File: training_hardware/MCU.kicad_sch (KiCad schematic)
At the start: 2 parts, among them J1 RJ45_LED_Shielded, U1 Teensy4.1_DEV-16771

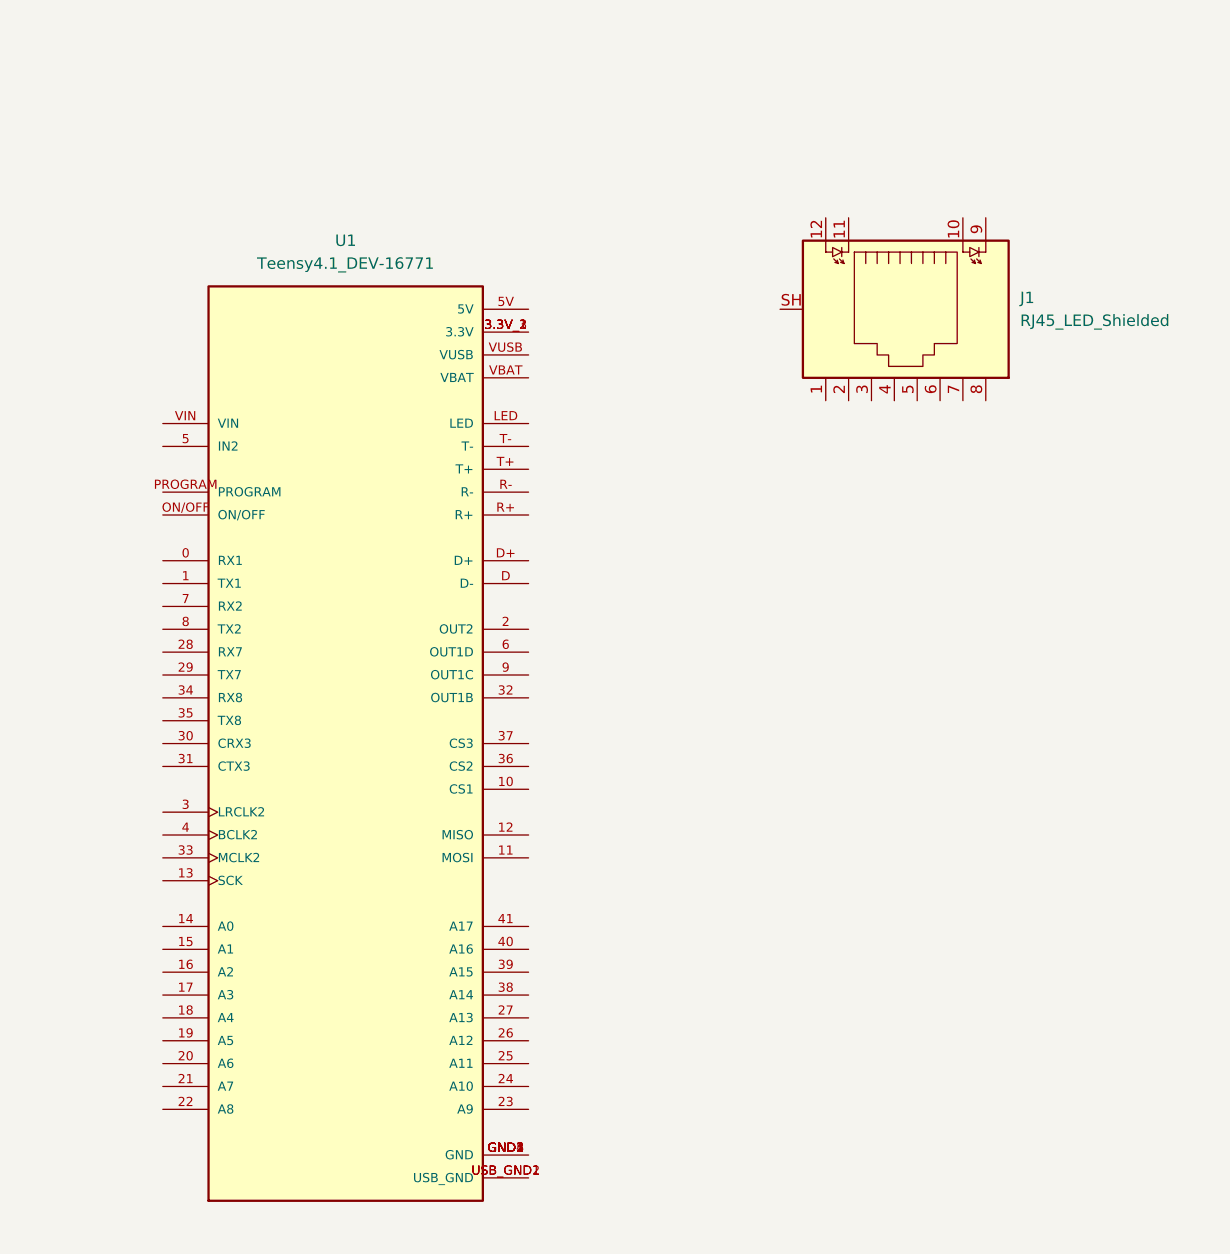
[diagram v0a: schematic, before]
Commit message: Add Ethernet
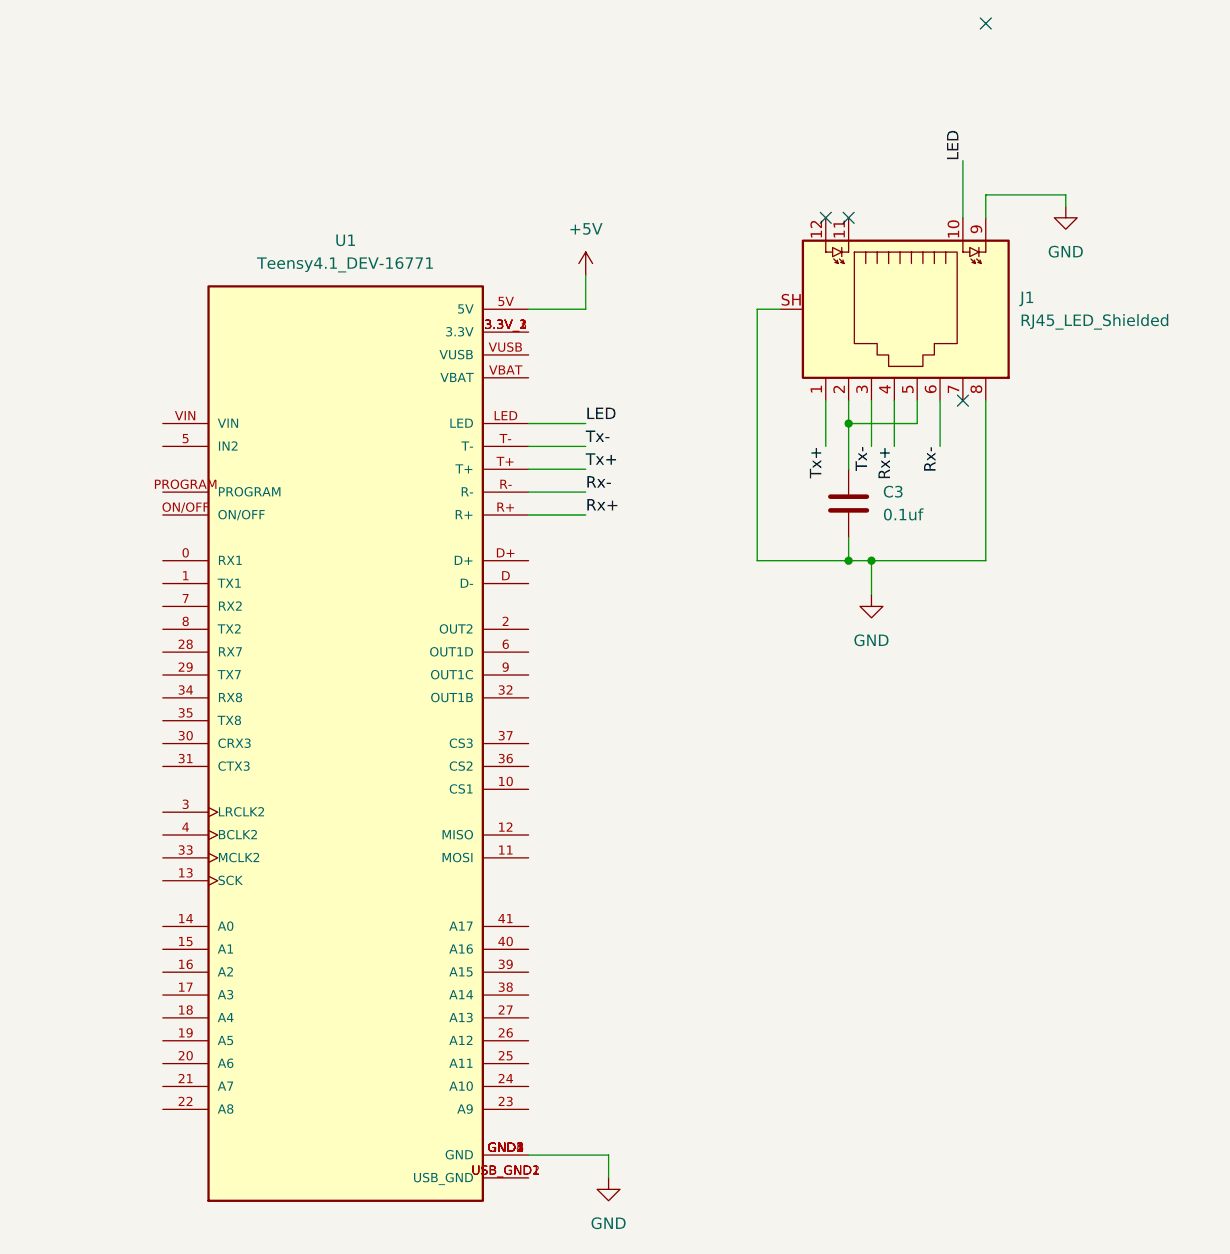
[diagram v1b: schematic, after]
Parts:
- added C3: 0.1uf, symbol Device:C
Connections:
- net Tx+: now reaches J1.1
- net Tx+: now also U1.T+
- net LED: now reaches J1.10
- net LED: now also U1.LED
- net at J1.2: now also J1.5, C3.1
- net Tx-: now reaches J1.3
- net Tx-: now also U1.T-
- net Rx+: now reaches J1.4
- net Rx+: now also U1.R+
- net Rx-: now reaches J1.6
- net Rx-: now also U1.R-
- net GND: now reaches J1.8
- net GND: now also J1.9, J1.SH, U1.GND1 (GND), U1.GND2 (GND), U1.GND3 (GND), U1.GND4 (GND), U1.GND5 (GND), C3.2
- net +5V: now reaches U1.5V
- no-connect marks 0 -> 4

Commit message: Finish Schematic
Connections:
- net STBY: now reaches U1.2 (OUT2)
- net CTX1: now reaches U1.22 (A8)
- net CRX1: now reaches U1.23 (A9)
- net +3V3: now reaches U1.3.3V_1 (3.3V), U1.3.3V_2 (3.3V), U1.3.3V_3 (3.3V)
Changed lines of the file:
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@@
+	(wire
+		(pts
+			(xy 165.1 52.07) (xy 176.53 52.07)
+		)
+		(stroke
+			(width 0)
+			(type default)
+		)
+	)
 	(wire
 		(pts
@@
 	(wire
 		(pts
+			(xy 115.57 138.43) (xy 124.46 138.43)
+		)
+		(stroke
+			(width 0)
+			(type default)
+		)
+	)
+	(wire
+		(pts
 			(xy 165.1 62.23) (xy 171.45 62.23)
 		)
@@
 	(wire
 		(pts
+			(xy 165.1 138.43) (xy 171.45 138.43)
+		)
+		(stroke
+			(width 0)
+			(type default)
+		)
+	)
+	(wire
+		(pts
 			(xy 173.99 143.51) (xy 173.99 146.05)
 		)
@@
 	(wire
 		(pts
+			(xy 165.1 85.09) (xy 173.99 85.09)
+		)
+		(stroke
+			(width 0)
+			(type default)
+		)
+	)
+	(wire
+		(pts
 			(xy 165.1 143.51) (xy 173.99 143.51)
 		)
@@
 		(pts
 			(xy 200.66 77.47) (xy 203.2 77.47)
+		)
+		(stroke
+			(width 0)
+			(type default)
+		)
+	)
+	(wire
+		(pts
+			(xy 176.53 45.72) (xy 176.53 52.07)
 		)
 		(stroke
@@
 			)
 			(justify right bottom)
+		)
+	)
+	(hierarchical_label "CRX1"
+		(shape input)
+		(at 171.45 138.43 0)
+		(effects
+			(font
+				(size 1.27 1.27)
+			)
+			(justify left)
+		)
+	)
+	(hierarchical_label "STBY"
+		(shape output)
+		(at 173.99 85.09 0)
+		(effects
+			(font
+				(size 1.27 1.27)
+			)
+			(justify left)
+		)
+	)
+	(hierarchical_label "CTX1"
+		(shape output)
+		(at 115.57 138.43 180)
+		(effects
+			(font
+				(size 1.27 1.27)
+			)
+			(justify right)
 		)
 	)
@@
 					(unit 1)
 				)
+			)
+		)
+	)
+	(symbol
+		(lib_id "power:+3V3")
+		(at 176.53 45.72 0)
+		(unit 1)
+		(exclude_from_sim no)
+		(in_bom yes)
+		(on_board yes)
+		(dnp no)
+		(fields_autoplaced yes)
+		(property "Reference" "#PWR016"
+			(at 176.53 49.53 0)
+			(effects
+				(font
+					(size 1.27 1.27)
+				)
+				(hide yes)
+			)
+		)
+		(property "Value" "+3V3"
+			(at 176.53 40.64 0)
+			(effects
+				(font
+					(size 1.27 1.27)
+				)
+			)
+		)
+		(property "Footprint" ""
+			(at 176.53 45.72 0)
+			(effects
+				(font
+					(size 1.27 1.27)
+				)
+				(hide yes)
+			)
+		)
+		(property "Datasheet" ""
+			(at 176.53 45.72 0)
+			(effects
+				(font
+					(size 1.27 1.27)
+				)
+				(hide yes)
+			)
+		)
+		(property "Description" "Power symbol creates a global label with name \"+3V3\""
+			(at 176.53 45.72 0)
+			(effects
+				(font
+					(size 1.27 1.27)
+				)
+				(hide yes)
+			)
+		)
+		(pin "1"
+		)
+		(instances
+			(project ""
+				(path "/4cf2d799-67ae-4e4e-ac38-46710a69e750/054b5761-e6bf-4667-8fab-116ffb3b3fc9"
+					(reference "#PWR016")
+					(unit 1)
+				)

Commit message: Layout Training
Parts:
- C3: footprint (none) -> Capacitor_SMD:C_0603_1608Metric
- J1: footprint (none) -> MRDT_Connectors:RJ45_Teensy
- U1: footprint MODULE_DEV-16771 -> MRDT_Shields:Teensy_4_1_Ethernet
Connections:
- net +5V: now also U1.VIN
- no-connect marks 4 -> 49
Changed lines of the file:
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@@
+	)
+	(no_connect
+		(at 165.1 77.47)
+	)
+	(no_connect
+		(at 124.46 107.95)
+	)
+	(no_connect
+		(at 165.1 125.73)
 	)
 	(no_connect
@@
 	)
 	(no_connect
+		(at 124.46 130.81)
+	)
+	(no_connect
+		(at 124.46 87.63)
+	)
+	(no_connect
+		(at 165.1 118.11)
+	)
+	(no_connect
+		(at 124.46 110.49)
+	)
+	(no_connect
+		(at 165.1 135.89)
+	)
+	(no_connect
+		(at 165.1 54.61)
+	)
+	(no_connect
+		(at 165.1 110.49)
+	)
+	(no_connect
+		(at 124.46 125.73)
+	)
+	(no_connect
+		(at 165.1 123.19)
+	)
+	(no_connect
+		(at 165.1 90.17)
+	)
+	(no_connect
+		(at 124.46 69.85)
+	)
+	(no_connect
+		(at 165.1 120.65)
+	)
+	(no_connect
+		(at 124.46 105.41)
+	)
+	(no_connect
+		(at 124.46 128.27)
+	)
+	(no_connect
+		(at 165.1 97.79)
+	)
+	(no_connect
+		(at 165.1 100.33)
+	)
+	(no_connect
+		(at 165.1 133.35)
+	)
+	(no_connect
 		(at 198.12 39.37)
 	)
 	(no_connect
-		(at 215.9 17.78)
+		(at 124.46 123.19)
+	)
+	(no_connect
+		(at 124.46 97.79)
+	)
+	(no_connect
+		(at 124.46 80.01)
+	)
+	(no_connect
+		(at 165.1 80.01)
+	)
+	(no_connect
+		(at 165.1 87.63)
+	)
+	(no_connect
+		(at 124.46 135.89)
+	)
+	(no_connect
+		(at 124.46 85.09)
+	)
+	(no_connect
+		(at 124.46 92.71)
+	)
+	(no_connect
+		(at 124.46 90.17)
+	)
+	(no_connect
+		(at 124.46 72.39)
+	)
+	(no_connect
+		(at 124.46 77.47)
+	)
+	(no_connect
+		(at 165.1 107.95)
+	)
+	(no_connect
+		(at 124.46 113.03)
+	)
+	(no_connect
+		(at 124.46 100.33)
+	)
+	(no_connect
+		(at 165.1 102.87)
+	)
+	(no_connect
+		(at 124.46 64.77)
+	)
+	(no_connect
+		(at 165.1 92.71)
+	)
+	(no_connect
+		(at 124.46 118.11)
+	)
+	(no_connect
+		(at 124.46 95.25)
+	)
+	(no_connect
+		(at 124.46 82.55)
+	)
+	(no_connect
+		(at 124.46 120.65)
+	)
+	(no_connect
+		(at 165.1 57.15)
+	)
+	(no_connect
+		(at 124.46 133.35)
+	)
+	(no_connect
+		(at 165.1 146.05)
 	)
 	(no_connect
 		(at 213.36 59.69)
 	)
+	(no_connect
+		(at 165.1 130.81)
+	)
+	(no_connect
+		(at 165.1 128.27)
+	)
 	(wire
 		(pts
@@
 	(wire
 		(pts
+			(xy 115.57 62.23) (xy 115.57 55.88)
+		)
+		(stroke
+			(width 0)
+			(type default)
+		)
+	)
+	(wire
+		(pts
 			(xy 115.57 138.43) (xy 124.46 138.43)
+		)
+		(stroke
+			(width 0)
+			(type default)
+		)
+	)
+	(wire
+		(pts
+			(xy 115.57 62.23) (xy 124.46 62.23)
 		)
 		(stroke
@@
 			)
 		)
-		(property "Footprint" ""
+		(property "Footprint" "MRDT_Connectors:RJ45_Teensy"
 			(at 206.375 49.53 90)
 			(effects
@@
 			)
 		)
-		(property "Footprint" ""
+		(property "Footprint" "Capacitor_SMD:C_0603_1608Metric"
 			(at 201.6252 74.93 0)
 			(effects
@@
 			)
 		)
-		(property "Footprint" "MODULE_DEV-16771"
+		(property "Footprint" "MRDT_Shields:Teensy_4_1_Ethernet"
 			(at 198.12 105.41 0)
 			(effects
@@
 					(unit 1)
 				)
+			)
+		)
+	)
+	(symbol
+		(lib_id "power:+5V")
+		(at 115.57 55.88 0)
+		(unit 1)
+		(exclude_from_sim no)
+		(in_bom yes)
+		(on_board yes)
+		(dnp no)
+		(fields_autoplaced yes)
+		(property "Reference" "#PWR017"
+			(at 115.57 59.69 0)
+			(effects
+				(font
+					(size 1.27 1.27)
+				)
+				(hide yes)
+			)
+		)
+		(property "Value" "+5V"
+			(at 115.57 50.8 0)
+			(effects
+				(font
+					(size 1.27 1.27)
+				)
+			)
+		)
+		(property "Footprint" ""
+			(at 115.57 55.88 0)
+			(effects
+				(font
+					(size 1.27 1.27)
+				)
+				(hide yes)
+			)
+		)
+		(property "Datasheet" ""
+			(at 115.57 55.88 0)
+			(effects
+				(font
+					(size 1.27 1.27)
+				)
+				(hide yes)
+			)
+		)
+		(property "Description" "Power symbol creates a global label with name \"+5V\""
+			(at 115.57 55.88 0)
+			(effects
+				(font
+					(size 1.27 1.27)
+				)
+				(hide yes)
+			)
+		)
+		(pin "1"
+		)
+		(instances
+			(project "training_hardware"
+				(path "/4cf2d799-67ae-4e4e-ac38-46710a69e750/054b5761-e6bf-4667-8fab-116ffb3b3fc9"
+					(reference "#PWR017")
+					(unit 1)
+				)
